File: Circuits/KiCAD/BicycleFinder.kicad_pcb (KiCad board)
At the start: 2 copper layers, 76.4 x 40.2 mm, 10 parts, among them P1 CONN_14, P2 CONN_14, P3 CONN_7, SW1 SW_PUSH, U1 LITE_LITE

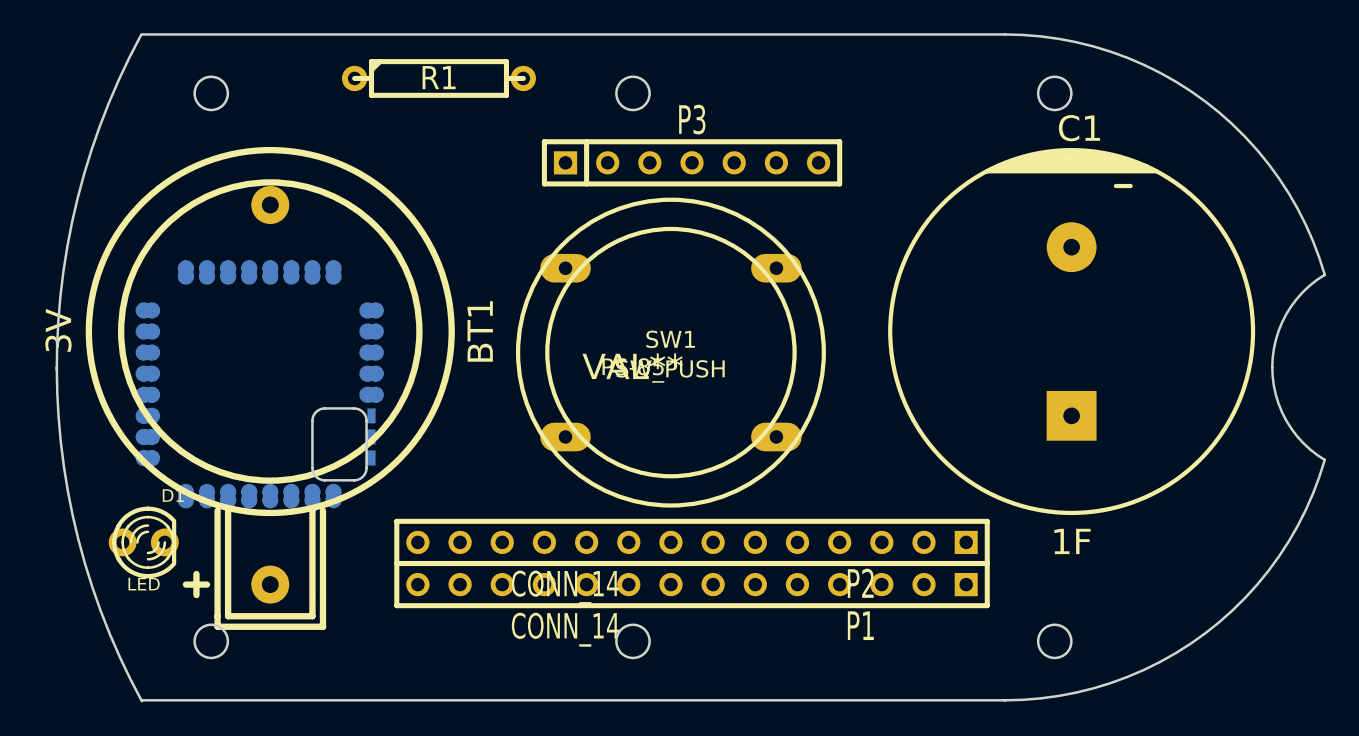
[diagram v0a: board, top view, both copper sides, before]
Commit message: Added an antenna shape in F.Silk layer.
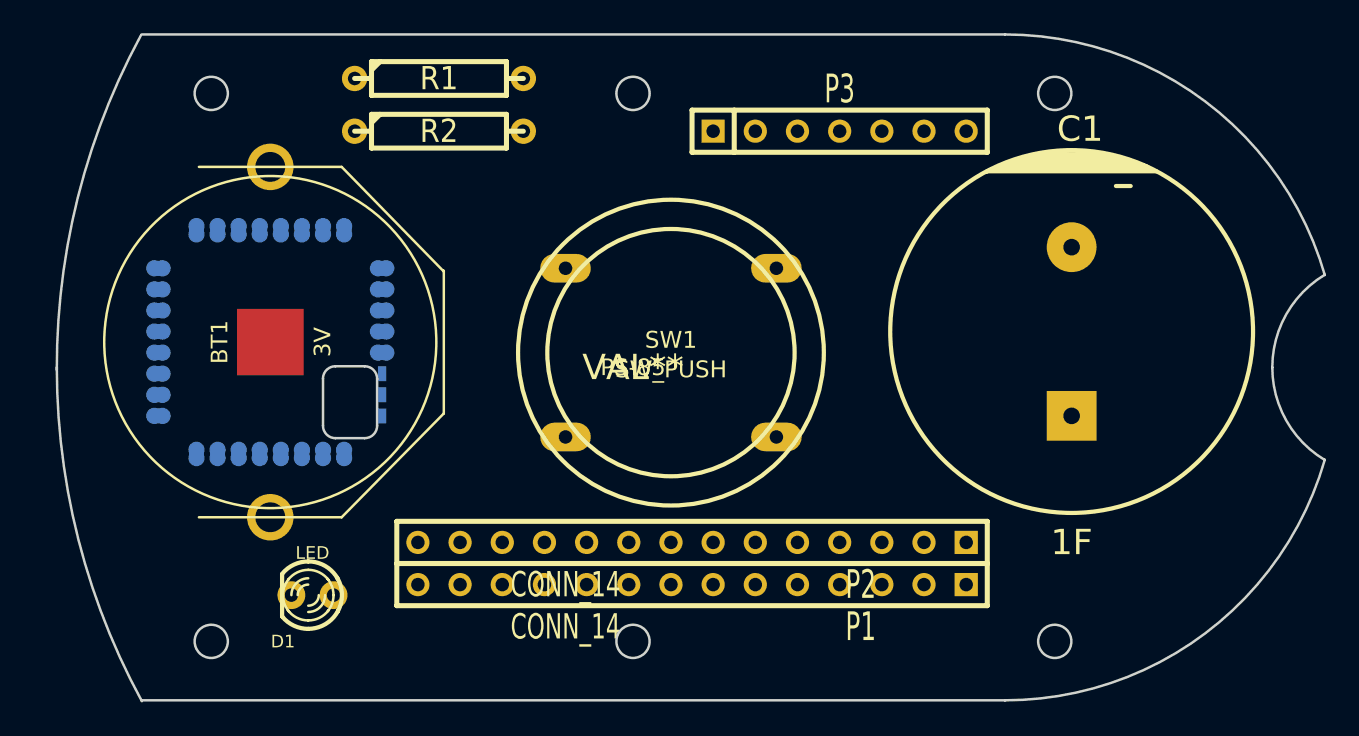
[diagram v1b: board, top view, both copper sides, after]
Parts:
- added R2: 1k, R4, F.Cu at (35.6, 18.4)
- BT1: footprint CR2032H -> BK-888
- moved D1 10.6 mm to (27.9, 46.4), turned to 180 degrees
- moved P3 9.09 mm to (59.7, 18.4)
- moved U1 2.62 mm to (18.4, 38.1)
- moved BT1 0.63 mm to (25.4, 31.1), turned to 90 degrees
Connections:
- BT1 pad 1: N-000001 -> /3V
- D1 pad 1: /Vcc -> N-000001
- R1 pad 1: N-000001 -> /3V

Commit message: Created a 3D shape of EDLC.
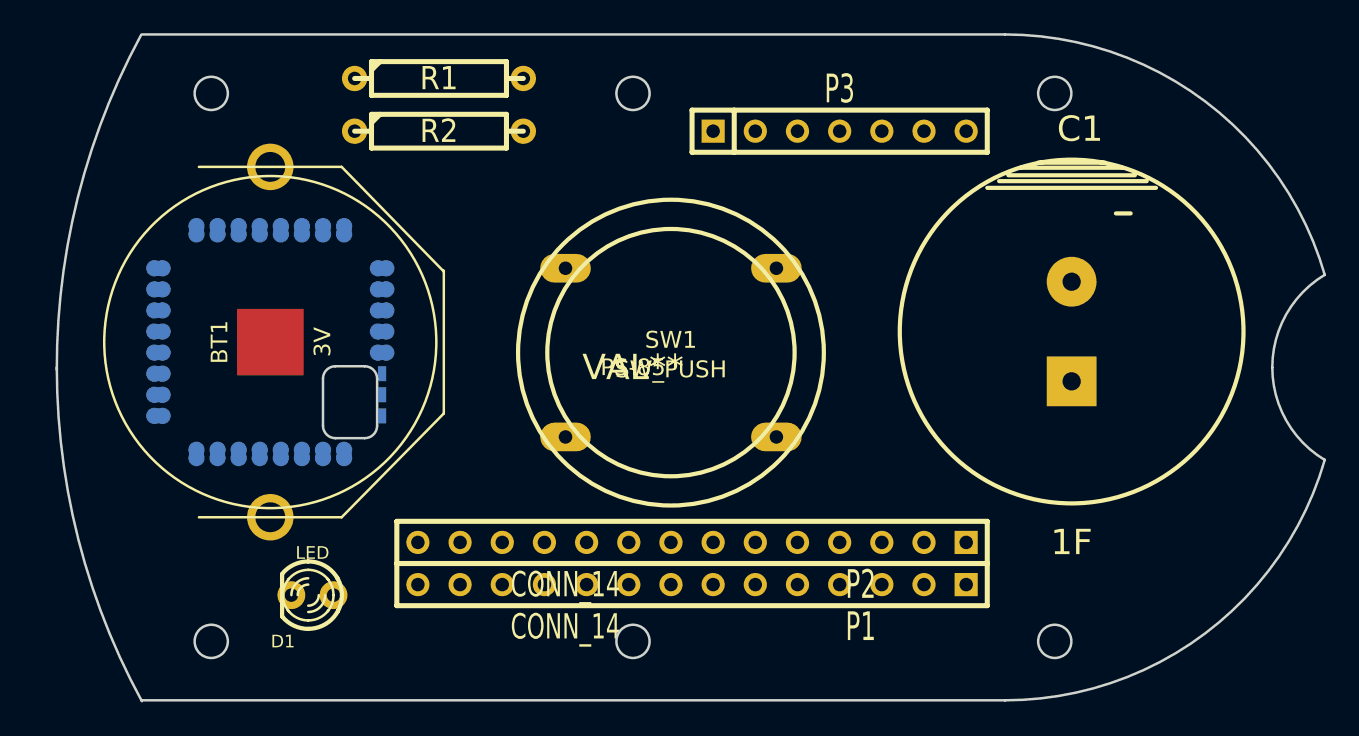
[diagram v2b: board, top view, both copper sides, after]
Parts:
- C1: footprint CP_22x41mm -> SE-5R5-D105VY
